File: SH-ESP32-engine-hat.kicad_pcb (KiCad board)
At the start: 4 copper layers, 34 x 52.8 mm, 109 parts, among them J301 Conn_02x04_Odd_Even, J302 Conn_02x04_Odd_Even, J401 I2C_top, J402 I2C_bottom, J403 GPIO subset, J501 Conn_02x04_Odd_Even, J502 Conn_02x04, Q501 S9015, Q502 S9015, Q503 S9015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

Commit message: Bump version number
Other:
- board text added: "Engine Top Hat Rev 0.2.1"
- board text removed: "Engine Top Hat Rev 0.2.0"
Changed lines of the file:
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@@
   (title_block
     (title "Engine Top Hat for SH-ESP32")
-    (date 2021-04-27)
-    (rev 0.1.0)
+    (date 2021-09-13)
+    (rev 0.2.1)
     (company "Hat Labs Ltd")
     (comment 1 https://creativecommons.org/licenses/by-sa/4.0)
@@
     (effects (font (size 1 1) (thickness 0.16)))
   )
-  (gr_text "Engine Top Hat\nRev 0.2.0" (at 157.8 79.5 90) (layer F.SilkS)
+  (gr_text "Engine Top Hat\nRev 0.2.1" (at 157.8 79.5 90) (layer F.SilkS)
     (effects (font (size 1 1) (thickness 0.16)) (justify left))
   )
-  (gr_text "Engine Top Hat\nRev 0.2.0" (at 154 80.4 270) (layer B.SilkS)
+  (gr_text "Engine Top Hat\nRev 0.2.1" (at 154 80.4 -90) (layer B.SilkS)
     (effects (font (size 1 1) (thickness 0.16)) (justify left mirror))
   )

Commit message: Save in KiCad 6 format
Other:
- net class Default removed

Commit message: Fix DRC errors
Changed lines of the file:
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@@
   (via (at 156.3 91.9) (size 0.6) (drill 0.4) (layers "F.Cu" "B.Cu") (net 4))
   (via (at 151.4 101.4) (size 0.6) (drill 0.4) (layers "F.Cu" "B.Cu") (net 4))
-  (segment (start 156.3 91.9) (end 156.3 92.4) (width 0.4) (layer "B.Cu") (net 4))
+  (segment (start 152.3 96.7) (end 152.3 100.5) (width 0.4) (layer "B.Cu") (net 4))
+  (segment (start 156.3 91.9) (end 156.3 92.7) (width 0.4) (layer "B.Cu") (net 4))
+  (segment (start 156.3 92.7) (end 152.3 96.7) (width 0.4) (layer "B.Cu") (net 4))
   (segment (start 152.3 100.5) (end 151.4 101.4) (width 0.4) (layer "B.Cu") (net 4))
-  (segment (start 156.3 92.4) (end 152.3 96.4) (width 0.4) (layer "B.Cu") (net 4))
-  (segment (start 152.3 96.4) (end 152.3 100.5) (width 0.4) (layer "B.Cu") (net 4))
   (segment (start 134.125 69.4875) (end 134.0875 69.45) (width 0.4) (layer "F.Cu") (net 5))
   (segment (start 131.615 73.66) (end 134.125 71.15) (width 0.4) (layer "F.Cu") (net 5))
@@
   (via (at 141.7 90.8) (size 0.6) (drill 0.4) (layers "F.Cu" "B.Cu") (net 30))
   (via (at 130.972992 105.826992) (size 0.6) (drill 0.4) (layers "F.Cu" "B.Cu") (net 30))
+  (segment (start 131.754013 105.045971) (end 130.972992 105.826992) (width 0.4) (layer "B.Cu") (net 30))
   (segment (start 141.7 90.8) (end 138.67327 90.8) (width 0.4) (layer "B.Cu") (net 30))
-  (segment (start 131.272991 105.526993) (end 130.972992 105.826992) (width 0.4) (layer "B.Cu") (net 30))
-  (segment (start 131.754013 97.719257) (end 131.754012 98.519258) (width 0.4) (layer "B.Cu") (net 30))
-  (segment (start 131.754012 98.519258) (end 131.454012 98.819258) (width 0.4) (layer "B.Cu") (net 30))
-  (segment (start 131.454012 98.819258) (end 131.454012 105.345972) (width 0.4) (layer "B.Cu") (net 30))
   (segment (start 138.67327 90.8) (end 131.754013 97.719257) (width 0.4) (layer "B.Cu") (net 30))
-  (segment (start 131.454012 105.345972) (end 131.272991 105.526993) (width 0.4) (layer "B.Cu") (net 30))
-  (segment (start 128.822999 105.452737) (end 129.115304 105.160432) (width 0.4) (layer "F.Cu") (net 31))
+  (segment (start 131.754013 97.719257) (end 131.754013 105.045971) (width 0.4) (layer "B.Cu") (net 30))
+  (segment (start 128.822999 106.186601) (end 128.936398 106.3) (width 0.4) (layer "F.Cu") (net 31))
+  (segment (start 128.936398 106.3) (end 129.454696 106.3) (width 0.4) (layer "F.Cu") (net 31))
+  (segment (start 128.822999 105.452737) (end 128.822999 106.186601) (width 0.4) (layer "F.Cu") (net 31))
+  (segment (start 129.575736 104.7) (end 128.822999 105.452737) (width 0.4) (layer "F.Cu") (net 31))
   (segment (start 140.95 86.29) (end 141.69 86.29) (width 0.4) (layer "F.Cu") (net 31))
-  (segment (start 128.822999 106.186601) (end 128.822999 105.452737) (width 0.4) (layer "F.Cu") (net 31))
   (segment (start 139.95 86.29) (end 140.95 86.29) (width 0.4) (layer "F.Cu") (net 31))
-  (segment (start 129.115304 105.160432) (end 130.682772 105.160432) (width 0.4) (layer "F.Cu") (net 31))
-  (segment (start 129.454696 106.3) (end 128.936398 106.3) (width 0.4) (layer "F.Cu") (net 31))
-  (segment (start 128.936398 106.3) (end 128.822999 106.186601) (width 0.4) (layer "F.Cu") (net 31))
   (segment (start 140.95 86.29) (end 140.95 85.28) (width 0.4) (layer "F.Cu") (net 31))
+  (segment (start 130.682772 104.7) (end 129.575736 104.7) (width 0.4) (layer "F.Cu") (net 31))
   (segment (start 141.69 86.29) (end 141.7 86.3) (width 0.4) (layer "F.Cu") (net 31))
-  (via (at 130.682772 105.160432) (size 0.6) (drill 0.4) (layers "F.Cu" "B.Cu") (net 31))
+  (via (at 130.682772 104.7) (size 0.6) (drill 0.4) (layers "F.Cu" "B.Cu") (net 31))
   (via (at 141.7 86.3) (size 0.6) (drill 0.4) (layers "F.Cu" "B.Cu") (net 31))
-  (segment (start 130.682772 104.736168) (end 130.682772 105.160432) (width 0.4) (layer "B.Cu") (net 31))
+  (segment (start 141.7 86.3) (end 138.8 86.3) (width 0.4) (layer "B.Cu") (net 31))
+  (segment (start 131.1 104.31894) (end 130.682772 104.736168) (width 0.4) (layer "B.Cu") (net 31))
+  (segment (start 131.227002 98.300962) (end 131.1 98.427964) (width 0.4) (layer "B.Cu") (net 31))
   (segment (start 131.227002 93.872998) (end 131.227002 98.300962) (width 0.4) (layer "B.Cu") (net 31))
-  (segment (start 130.927001 98.600963) (end 130.927001 104.491939) (width 0.4) (layer "B.Cu") (net 31))
-  (segment (start 131.227002 98.300962) (end 130.927001 98.600963) (width 0.4) (layer "B.Cu") (net 31))
   (segment (start 138.8 86.3) (end 131.227002 93.872998) (width 0.4) (layer "B.Cu") (net 31))
-  (segment (start 141.7 86.3) (end 138.8 86.3) (width 0.4) (layer "B.Cu") (net 31))
-  (segment (start 130.927001 104.491939) (end 130.682772 104.736168) (width 0.4) (layer "B.Cu") (net 31))
+  (segment (start 131.1 98.427964) (end 131.1 104.31894) (width 0.4) (layer "B.Cu") (net 31))
   (segment (start 144.06 71.75) (end 142.45 70.14) (width 0.4) (layer "F.Cu") (net 32))
   (segment (start 141.15 69.65) (end 141.96 69.65) (width 0.4) (layer "F.Cu") (net 32))
@@
   (segment (start 138.51 80.35) (end 138.51 80.36) (width 0.4) (layer "F.Cu") (net 35))
   (segment (start 144.19 79.37) (end 143.356636 80.203364) (width 0.4) (layer "F.Cu") (net 35))
-  (segment (start 143.356636 80.203364) (end 143.356636 77.45701) (width 0.4) (layer "F.Cu") (net 35))
+  (segment (start 143.356636 80.203364) (end 143.356636 77.843364) (width 0.4) (layer "F.Cu") (net 35))
+  (segment (start 143.356636 77.843364) (end 143.5 77.7) (width 0.4) (layer "F.Cu") (net 35))
   (segment (start 145.65 79.37) (end 144.19 79.37) (width 0.4) (layer "F.Cu") (net 35))
   (segment (start 139.7 81.55) (end 141.2 81.55) (width 0.4) (layer "F.Cu") (net 35))
   (segment (start 142.01 81.55) (end 143.356636 80.203364) (width 0.4) (layer "F.Cu") (net 35))
   (segment (start 138.51 80.36) (end 139.7 81.55) (width 0.4) (layer "F.Cu") (net 35))
-  (via (at 143.356636 77.45701) (size 0.6) (drill 0.4) (layers "F.Cu" "B.Cu") (net 35))
-  (segment (start 143.356636 77.443364) (end 143.356636 77.45701) (width 0.4) (layer "B.Cu") (net 35))
-  (segment (start 143.5 60.06) (end 143.5 77.3) (width 0.4) (layer "B.Cu") (net 35))
-  (segment (start 142.24 58.8) (end 143.5 60.06) (width 0.4) (layer "B.Cu") (net 35))
-  (segment (start 143.5 77.3) (end 143.356636 77.443364) (width 0.4) (layer "B.Cu") (net 35))
+  (via (at 143.5 77.7) (size 0.6) (drill 0.4) (layers "F.Cu" "B.Cu") (net 35))
+  (segment (start 143.5 77.7) (end 143.5 60.06) (width 0.4) (layer "B.Cu") (net 35))
+  (segment (start 143.5 60.06) (end 142.24 58.8) (width 0.4) (layer "B.Cu") (net 35))
   (segment (start 129.7 107.3) (end 130.6 107.3) (width 0.25) (layer "F.Cu") (net 36))
   (segment (start 130.6 107.3) (end 130.8 107.1) (width 0.25) (layer "F.Cu") (net 36))
@@
   (zone (net 1) (net_name "GND") (layer "F.Cu") (hatch edge 0.508)
     (connect_pads (clearance 0.2))
-    (min_thickness 0.2)
+    (min_thickness 0.2) (filled_areas_thickness no)
     (fill yes (thermal_gap 0.5) (thermal_bridge_width 0.5))
     (polygon
@@
   (zone (net 1) (net_name "GND") (layer "In1.Cu") (hatch edge 0.508)
     (connect_pads (clearance 0.2))
-    (min_thickness 0.2)
+    (min_thickness 0.2) (filled_areas_thickness no)
     (fill yes (thermal_gap 0.5) (thermal_bridge_width 0.5))
     (polygon
@@
   (zone (net 2) (net_name "+3V3") (layer "In2.Cu") (hatch edge 0.508)
     (connect_pads (clearance 0.2))
-    (min_thickness 0.2)
+    (min_thickness 0.2) (filled_areas_thickness no)
     (fill yes (thermal_gap 0.5) (thermal_bridge_width 0.5))
     (polygon
@@
   (zone (net 1) (net_name "GND") (layer "B.Cu") (hatch edge 0.508)
     (connect_pads (clearance 0.2))
-    (min_thickness 0.2)
+    (min_thickness 0.2) (filled_areas_thickness no)
     (fill yes (thermal_gap 0.5) (thermal_bridge_width 0.5))
     (polygon

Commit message: Bump the version number
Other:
- board text added: "Engine Top Hat Rev 1.0.0"
- board text removed: "Engine Top Hat Rev 0.2.1"
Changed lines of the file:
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@@
   (title_block
     (title "Engine Top Hat for SH-ESP32")
-    (date "2021-09-13")
-    (rev "0.2.1")
+    (date "2021-12-31")
+    (rev "1.0.0")
     (company "Hat Labs Ltd")
     (comment 1 "https://creativecommons.org/licenses/by-sa/4.0")
@@
     (effects (font (size 0.8 0.8) (thickness 0.16)) (justify right mirror))
   )
-  (gr_text "Engine Top Hat\nRev 0.2.1" (at 154 80.4 -90) (layer "B.SilkS")
+  (gr_text "Engine Top Hat\nRev 1.0.0" (at 154 80.4 -90) (layer "B.SilkS")
     (effects (font (size 1 1) (thickness 0.16)) (justify left mirror))
   )
@@
     (effects (font (size 0.8 0.8) (thickness 0.16)))
   )
-  (gr_text "Engine Top Hat\nRev 0.2.1" (at 157.8 79.5 90) (layer "F.SilkS")
+  (gr_text "Engine Top Hat\nRev 1.0.0" (at 157.8 79.5 90) (layer "F.SilkS")
     (effects (font (size 1 1) (thickness 0.16)) (justify left))
   )

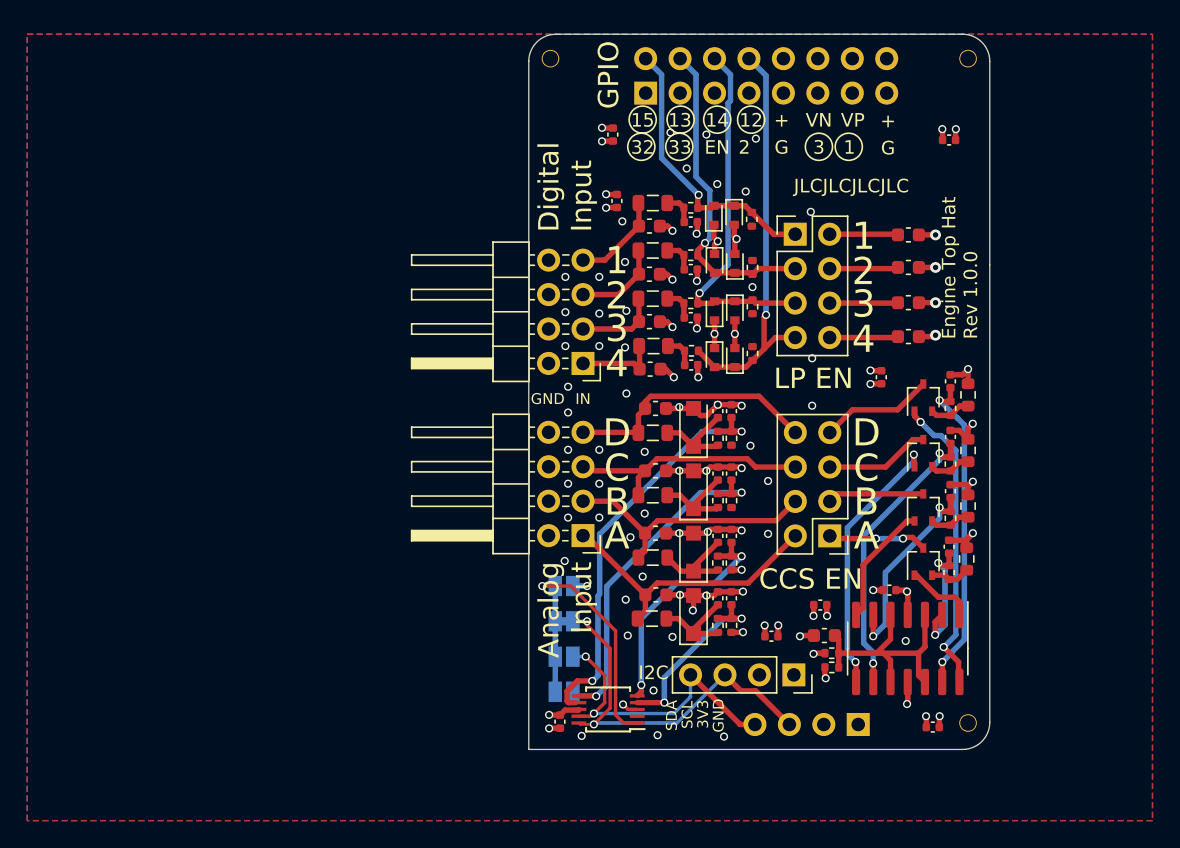
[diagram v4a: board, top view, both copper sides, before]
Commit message: Remove tooling holes
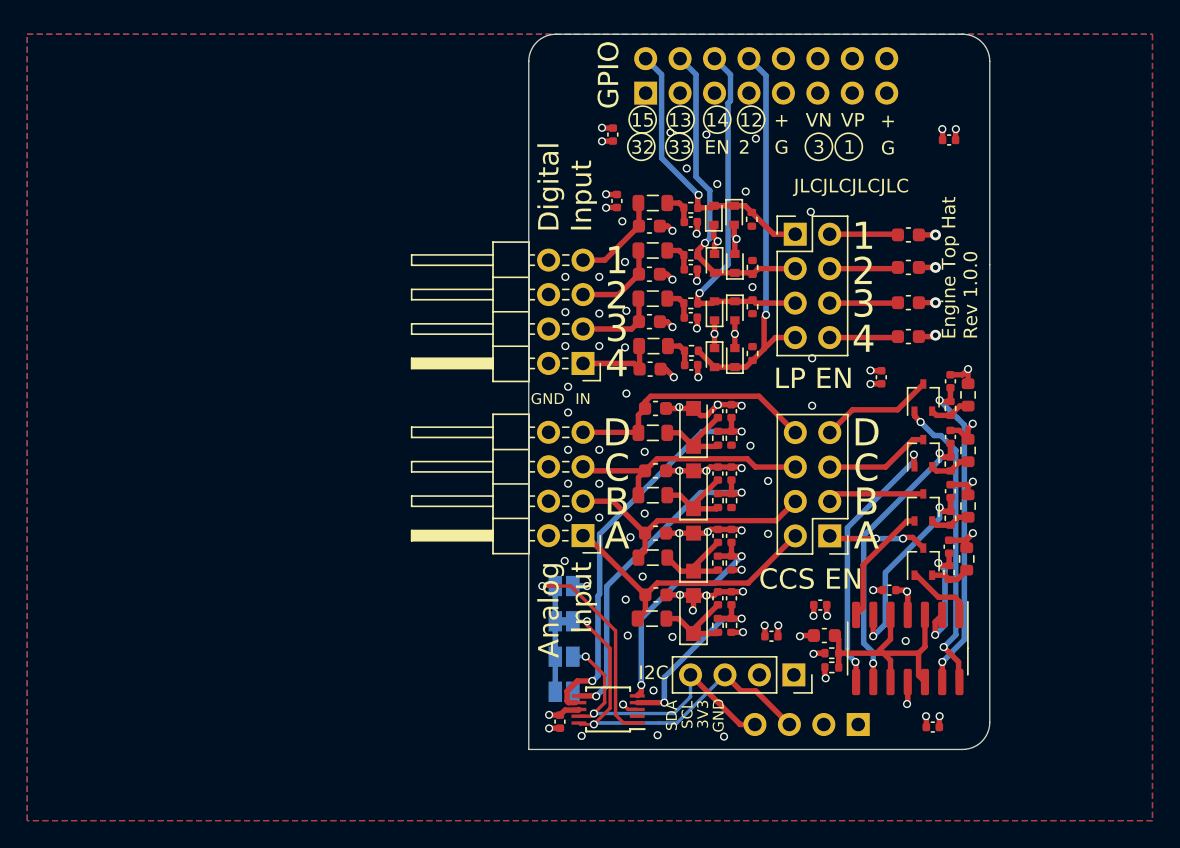
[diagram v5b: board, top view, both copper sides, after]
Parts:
- removed H201, H202, H203: Tooling hole, SH-ESP32-tank-hat:JlcpcbToolingHole
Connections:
- J403 pad 1: (no net) -> unconnected-(J403-Pad1)
- J403 pad 11: (no net) -> unconnected-(J403-Pad11)
- J403 pad 12: (no net) -> unconnected-(J403-Pad12)
- J403 pad 13: (no net) -> unconnected-(J403-Pad13)
- J403 pad 14: (no net) -> unconnected-(J403-Pad14)
- J403 pad 3: (no net) -> unconnected-(J403-Pad3)
- J403 pad 5: (no net) -> unconnected-(J403-Pad5)
- J403 pad 7: (no net) -> unconnected-(J403-Pad7)
- U502 pad 2: (no net) -> unconnected-(U502-Pad2)
